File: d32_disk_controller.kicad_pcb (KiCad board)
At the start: 2 copper layers, 107.5 x 80.3 mm, 25 parts, among them J1 Clock_Test, J2 IDC_Floppy, J3 EDGE, U1 27C64, U2 WD2797, U3 74HCT174, U4 74HCT139, U5 74HCT00, U6 74HCT04, U7 74LS07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

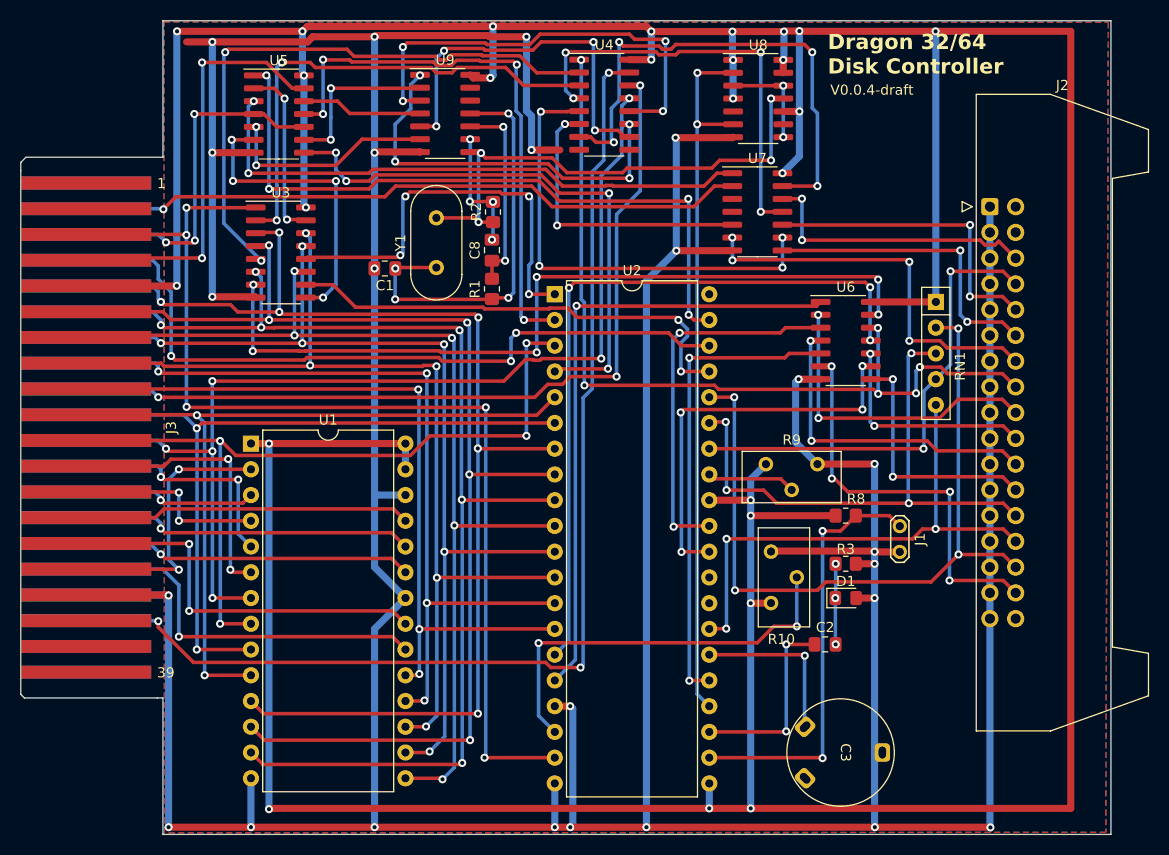
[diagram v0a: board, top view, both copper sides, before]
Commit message: update from component selection change
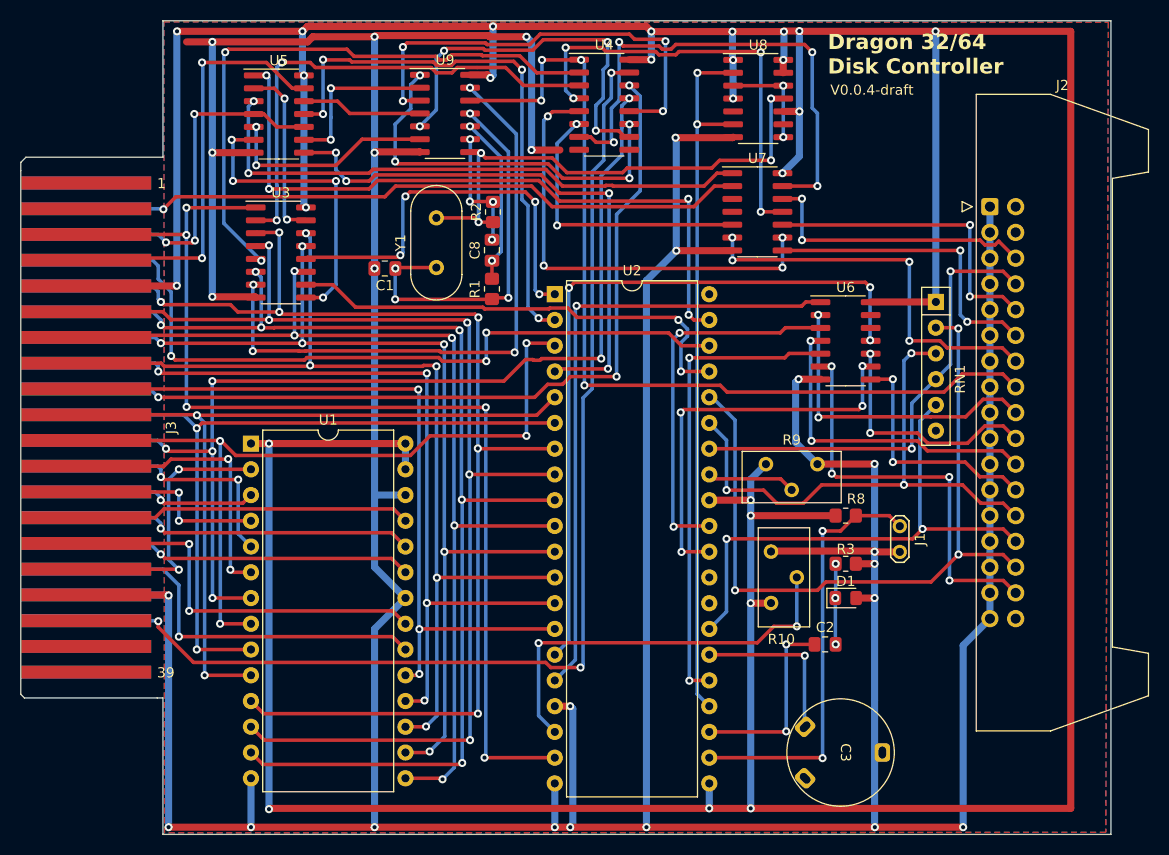
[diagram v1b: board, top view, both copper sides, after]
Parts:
- J1: value Clock_Test -> ~{TEST}
- RN1: value 150R -> 220R; footprint Resistor_THT:R_Array_SIP5 -> Resistor_THT:R_Array_SIP6
- U6: value 74HCT04 -> 74LS06
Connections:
- U6 pad 12: MOTOR -> unconnected-(U6-Pad12)
- U6 pad 13: Net-(U3-Q2) -> unconnected-(U6-Pad13)
- U9 pad 12: unconnected-(U9-Pad12) -> MOTOR
- U9 pad 13: unconnected-(U9-Pad13) -> Net-(U3-Q2)
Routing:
- net Net-(U3-Q2): track 80.2 -> 60.6 mm, vias 6 -> 4
- net MOTOR: track 85.6 -> 91.3 mm, vias 6 -> 4
- net Net-(C8-Pad1): track 19.6 -> 16.7 mm
- net Net-(C1-Pad1): track 40.8 -> 38.1 mm
- net ~{STEP}: track 21.7 -> 23.8 mm
- net GND: track 524.7 -> 523.1 mm
- net ~{WPRT}: track 75.8 -> 74.5 mm, vias 4 -> 3
- net ~{IP}: track 55.4 -> 54.1 mm, vias 4 -> 3
- net ~{WE}: track 55.6 -> 54.5 mm
- net Net-(U4B-O2): track 37.1 -> 38.0 mm
- net ~{WG}: track 24.5 -> 23.6 mm
- net ENP: track 40.5 -> 39.7 mm
- net ~{TR00}: track 46.7 -> 46.0 mm
- net Net-(U4A-O2): track 29.0 -> 28.4 mm
- net Net-(U4A-O0): track 42.8 -> 43.5 mm
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
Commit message: add test points
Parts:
- added J4: ~{MR}, TestPoint:TestPoint_2Pads_Pitch2.54mm_Drill0.8mm, F.Cu at (95.9, 118.8)
- added TP1: TestPoint_WD, TestPoint:TestPoint_Loop_D2.50mm_Drill1.0mm, F.Cu at (121.8, 74.4)
- added TP2: TestPoint_TG43, TestPoint:TestPoint_Loop_D2.50mm_Drill1.0mm, F.Cu at (98.6, 102.6)
- added TP3: TestPoint_Probe, TestPoint:TestPoint_Loop_D2.50mm_Drill1.0mm, F.Cu at (98.6, 108.7)
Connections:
- U2 pad 29: unconnected-(U2-TG43-Pad29) -> TG43
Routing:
- net TG43: track 0.00 -> 21.2 mm
- net GND: track 523.1 -> 527.5 mm, vias 25 -> 26
- net DIRC: track 62.1 -> 66.4 mm
- net ~{RESET}: track 107.5 -> 109.9 mm
- net D7: track 75.7 -> 76.3 mm
